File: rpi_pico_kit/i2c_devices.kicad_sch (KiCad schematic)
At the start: 7 parts, among them J7 Conn_01x04_Male, J8 OLED Display, J9 Conn_01x04_Male, U10 AT24CS32

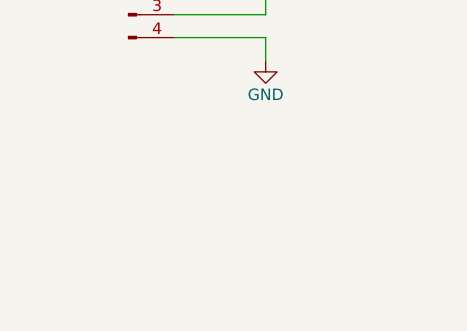
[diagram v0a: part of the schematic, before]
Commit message: added i2c interface for vga and dvi
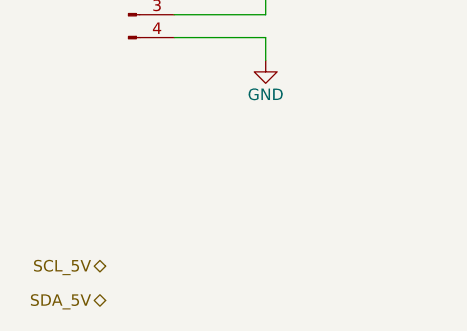
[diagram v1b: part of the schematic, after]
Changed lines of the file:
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@@
     (effects (font (size 1.27 1.27)) (justify right bottom))
+  )
+  (hierarchical_label "SDA_5V" (shape bidirectional) (at 81.28 143.51 180) (fields_autoplaced)
+    (effects (font (size 1.27 1.27)) (justify right))
+  )
+  (hierarchical_label "SCL_5V" (shape bidirectional) (at 81.28 139.7 180) (fields_autoplaced)
+    (effects (font (size 1.27 1.27)) (justify right))
   )
   (hierarchical_label "SDA" (shape bidirectional) (at 80.01 82.55 180) (fields_autoplaced)

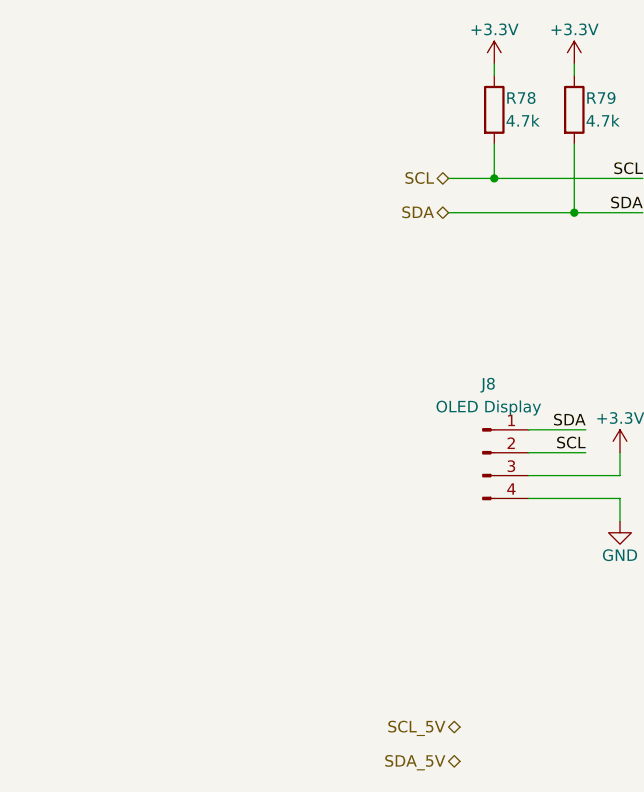
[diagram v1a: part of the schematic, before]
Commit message: added i2c level shifters
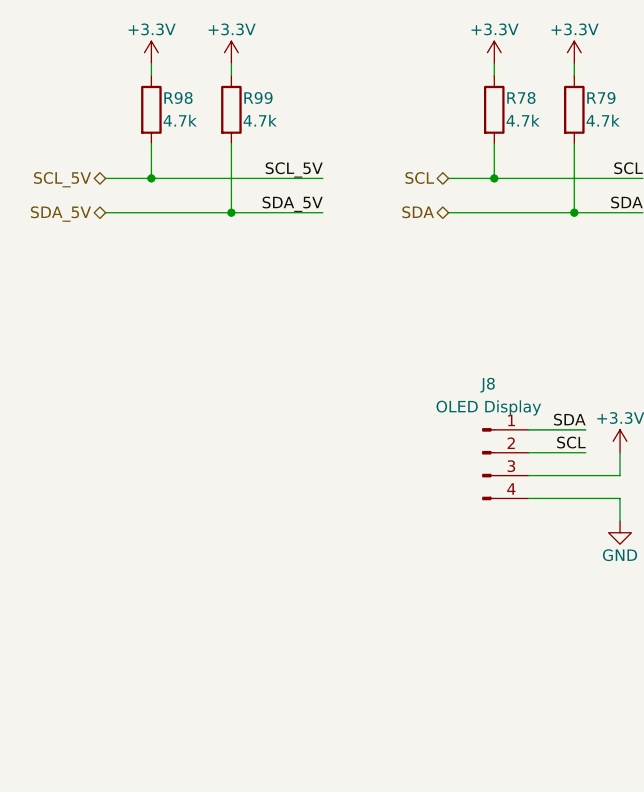
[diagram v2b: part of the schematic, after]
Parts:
- added R98, R99: 4.7k, Resistor_SMD:R_0805_2012Metric_Pad1.20x1.40mm_HandSolder, symbol Device:R
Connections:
- net +3V3: now also R98.1, R99.1
- net SCL_5V: now also R98.2
- net SDA_5V: now also R99.2
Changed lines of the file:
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@@
     (rev "1")
   )
+  (junction (at 46.99 78.74) (diameter 0) (color 0 0 0 0)
+  )
   (junction (at 209.55 86.36) (diameter 0) (color 0 0 0 0)
   )
@@
   (junction (at 93.98 82.55) (diameter 0) (color 0 0 0 0)
   )
+  (junction (at 55.88 82.55) (diameter 0) (color 0 0 0 0)
+  )
   (junction (at 85.09 78.74) (diameter 0) (color 0 0 0 0)
   )
@@
     (stroke (width 0) (type default))
   )
+  (wire (pts (xy 55.88 82.55) (xy 66.04 82.55))
+    (stroke (width 0) (type default))
+  )
   (wire (pts (xy 88.9 109.22) (xy 95.25 109.22))
     (stroke (width 0) (type default))
@@
     (stroke (width 0) (type default))
   )
+  (wire (pts (xy 41.91 78.74) (xy 46.99 78.74))
+    (stroke (width 0) (type default))
+  )
   (wire (pts (xy 219.71 101.6) (xy 222.25 101.6))
     (stroke (width 0) (type default))
@@
     (stroke (width 0) (type default))
   )
+  (wire (pts (xy 55.88 74.93) (xy 55.88 82.55))
+    (stroke (width 0) (type default))
+  )
   (wire (pts (xy 146.05 76.2) (xy 156.21 76.2))
     (stroke (width 0) (type default))
@@
     (stroke (width 0) (type default))
   )
+  (wire (pts (xy 46.99 78.74) (xy 66.04 78.74))
+    (stroke (width 0) (type default))
+  )
+  (wire (pts (xy 41.91 82.55) (xy 55.88 82.55))
+    (stroke (width 0) (type default))
+  )
+  (wire (pts (xy 46.99 66.04) (xy 46.99 67.31))
+    (stroke (width 0) (type default))
+  )
   (wire (pts (xy 219.71 96.52) (xy 229.87 96.52))
     (stroke (width 0) (type default))
@@
     (stroke (width 0) (type default))
   )
+  (wire (pts (xy 55.88 66.04) (xy 55.88 67.31))
+    (stroke (width 0) (type default))
+  )
   (wire (pts (xy 209.55 81.28) (xy 209.55 86.36))
     (stroke (width 0) (type default))
@@
     (stroke (width 0) (type default))
   )
+  (wire (pts (xy 46.99 74.93) (xy 46.99 78.74))
+    (stroke (width 0) (type default))
+  )
   (wire (pts (xy 199.39 96.52) (xy 196.85 96.52))
     (stroke (width 0) (type default))
@@
     (effects (font (size 1.27 1.27)) (justify right bottom))
   )
+  (label "SCL_5V" (at 66.04 78.74 0) (fields_autoplaced)
+    (effects (font (size 1.27 1.27)) (justify right bottom))
+  )
   (label "SCL" (at 156.21 109.22 0) (fields_autoplaced)
     (effects (font (size 1.27 1.27)) (justify right bottom))
@@
     (effects (font (size 1.27 1.27)) (justify right bottom))
   )
+  (label "SDA_5V" (at 66.04 82.55 0) (fields_autoplaced)
+    (effects (font (size 1.27 1.27)) (justify right bottom))
+  )
   (label "SDA" (at 156.21 81.28 0) (fields_autoplaced)
     (effects (font (size 1.27 1.27)) (justify right bottom))
   )
-  (hierarchical_label "SDA_5V" (shape bidirectional) (at 81.28 143.51 180) (fields_autoplaced)
+  (hierarchical_label "SDA_5V" (shape bidirectional) (at 41.91 82.55 180) (fields_autoplaced)
     (effects (font (size 1.27 1.27)) (justify right))
   )
-  (hierarchical_label "SCL_5V" (shape bidirectional) (at 81.28 139.7 180) (fields_autoplaced)
+  (hierarchical_label "SCL_5V" (shape bidirectional) (at 41.91 78.74 180) (fields_autoplaced)
     (effects (font (size 1.27 1.27)) (justify right))
   )
@@
     (effects (font (size 1.27 1.27)) (justify right))
   )
+  (symbol (lib_id "power:+3.3V") (at 46.99 66.04 0) (unit 1)
+    (in_bom yes) (on_board yes)
+    (property "Reference" "#PWR087" (id 0) (at 46.99 69.85 0)
+      (effects (font (size 1.27 1.27)) hide)
+    )
+    (property "Value" "+3.3V" (id 1) (at 46.99 62.23 0)
+      (effects (font (size 1.27 1.27)))
+    )
+    (property "Footprint" "" (id 2) (at 46.99 66.04 0)
+      (effects (font (size 1.27 1.27)) hide)
+    )
+    (property "Datasheet" "" (id 3) (at 46.99 66.04 0)
+      (effects (font (size 1.27 1.27)) hide)
+    )
+    (pin "1")
+  )
   (symbol (lib_id "Device:C") (at 217.17 86.36 90) (unit 1)
     (in_bom yes) (on_board yes)
@@
     )
     (property "Datasheet" "~" (id 3) (at 93.98 71.12 0)
+      (effects (font (size 1.27 1.27)) hide)
+    )
+    (pin "1")
+    (pin "2")
+  )
+  (symbol (lib_id "power:+3.3V") (at 55.88 66.04 0) (unit 1)
+    (in_bom yes) (on_board yes)
+    (property "Reference" "#PWR088" (id 0) (at 55.88 69.85 0)
+      (effects (font (size 1.27 1.27)) hide)
+    )
+    (property "Value" "+3.3V" (id 1) (at 55.88 62.23 0)
+      (effects (font (size 1.27 1.27)))
+    )
+    (property "Footprint" "" (id 2) (at 55.88 66.04 0)
+      (effects (font (size 1.27 1.27)) hide)
+    )
+    (property "Datasheet" "" (id 3) (at 55.88 66.04 0)
+      (effects (font (size 1.27 1.27)) hide)
+    )
+    (pin "1")
+  )
+  (symbol (lib_id "Device:R") (at 46.99 71.12 0) (unit 1)
+    (in_bom yes) (on_board yes)
+    (property "Reference" "R98" (id 0) (at 48.26 69.85 0)
+      (effects (font (size 1.27 1.27)) (justify left))
+    )
+    (property "Value" "4.7k" (id 1) (at 48.26 72.39 0)
+      (effects (font (size 1.27 1.27)) (justify left))
+    )
+    (property "Footprint" "Resistor_SMD:R_0805_2012Metric_Pad1.20x1.40mm_HandSolder" (id 2) (at 45.212 71.12 90)
+      (effects (font (size 1.27 1.27)) hide)
+    )
+    (property "Datasheet" "~" (id 3) (at 46.99 71.12 0)
       (effects (font (size 1.27 1.27)) hide)
     )
@@
     (pin "1")
   )
+  (symbol (lib_id "Device:R") (at 55.88 71.12 0) (unit 1)
+    (in_bom yes) (on_board yes)
+    (property "Reference" "R99" (id 0) (at 57.15 69.85 0)
+      (effects (font (size 1.27 1.27)) (justify left))
+    )
+    (property "Value" "4.7k" (id 1) (at 57.15 72.39 0)
+      (effects (font (size 1.27 1.27)) (justify left))
+    )
+    (property "Footprint" "Resistor_SMD:R_0805_2012Metric_Pad1.20x1.40mm_HandSolder" (id 2) (at 54.102 71.12 90)
+      (effects (font (size 1.27 1.27)) hide)
+    )
+    (property "Datasheet" "~" (id 3) (at 55.88 71.12 0)
+      (effects (font (size 1.27 1.27)) hide)
+    )
+    (pin "1")
+    (pin "2")
+  )
   (symbol (lib_id "power:GND") (at 196.85 104.14 0) (unit 1)

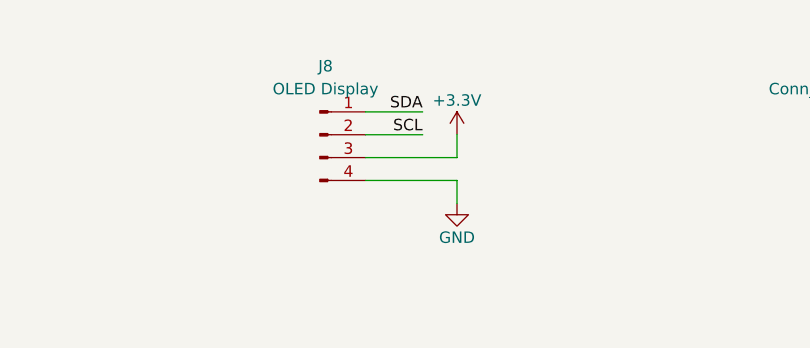
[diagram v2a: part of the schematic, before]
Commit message: added test pads for uart and swd of debugger
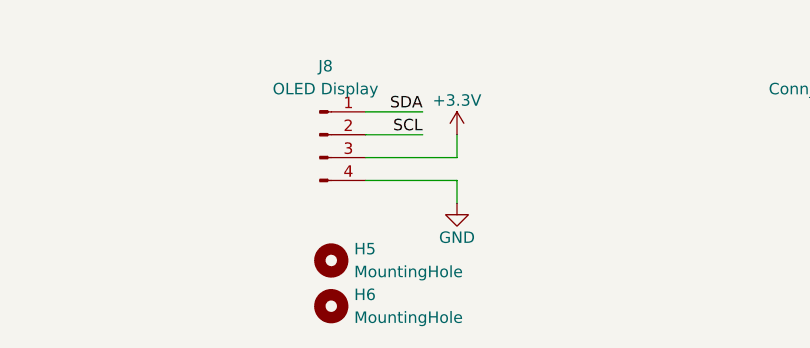
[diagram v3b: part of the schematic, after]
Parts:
- added H5, H6: MountingHole, MountingHole:MountingHole_2.7mm_M2.5, symbol Mechanical:MountingHole
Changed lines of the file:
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@@
     (effects (font (size 1.27 1.27)) (justify right))
+  )
+  (symbol (lib_id "Mechanical:MountingHole") (at 85.09 128.27 0) (unit 1)
+    (in_bom yes) (on_board yes) (fields_autoplaced)
+    (property "Reference" "H6" (id 0) (at 87.63 126.9999 0)
+      (effects (font (size 1.27 1.27)) (justify left))
+    )
+    (property "Value" "MountingHole" (id 1) (at 87.63 129.5399 0)
+      (effects (font (size 1.27 1.27)) (justify left))
+    )
+    (property "Footprint" "MountingHole:MountingHole_2.7mm_M2.5" (id 2) (at 85.09 128.27 0)
+      (effects (font (size 1.27 1.27)) hide)
+    )
+    (property "Datasheet" "~" (id 3) (at 85.09 128.27 0)
+      (effects (font (size 1.27 1.27)) hide)
+    )
   )
   (symbol (lib_id "power:+3.3V") (at 46.99 66.04 0) (unit 1)
@@
     (pin "1")
   )
+  (symbol (lib_id "Mechanical:MountingHole") (at 85.09 123.19 0) (unit 1)
+    (in_bom yes) (on_board yes) (fields_autoplaced)
+    (property "Reference" "H5" (id 0) (at 87.63 121.9199 0)
+      (effects (font (size 1.27 1.27)) (justify left))
+    )
+    (property "Value" "MountingHole" (id 1) (at 87.63 124.4599 0)
+      (effects (font (size 1.27 1.27)) (justify left))
+    )
+    (property "Footprint" "MountingHole:MountingHole_2.7mm_M2.5" (id 2) (at 85.09 123.19 0)
+      (effects (font (size 1.27 1.27)) hide)
+    )
+    (property "Datasheet" "~" (id 3) (at 85.09 123.19 0)
+      (effects (font (size 1.27 1.27)) hide)
+    )
+  )
 )

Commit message: added some MPNs, added fiducials
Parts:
- U10: Manufacturer Part Number (none) -> CAT24C32WI-GT3; Supplier (none) -> Digikey; Supplier Part URL (none) -> https://www.digikey.cz/en/products/detail/onsemi/CAT24C32WI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
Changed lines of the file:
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@@
+      (effects (font (size 1.27 1.27)) hide)
+    )
+    (property "Manufacturer Part Number" "CAT24C32WI-GT3" (id 4) (at 209.55 99.06 0)
+      (effects (font (size 1.27 1.27)) hide)
+    )
+    (property "Supplier" "Digikey" (id 5) (at 209.55 99.06 0)
+      (effects (font (size 1.27 1.27)) hide)
+    )
+    (property "Supplier Part URL" "https://www.digikey.cz/en/products/detail/onsemi/CAT24C32WI-GT3/1631007" (id 6) (at 209.55 99.06 0)
       (effects (font (size 1.27 1.27)) hide)
     )

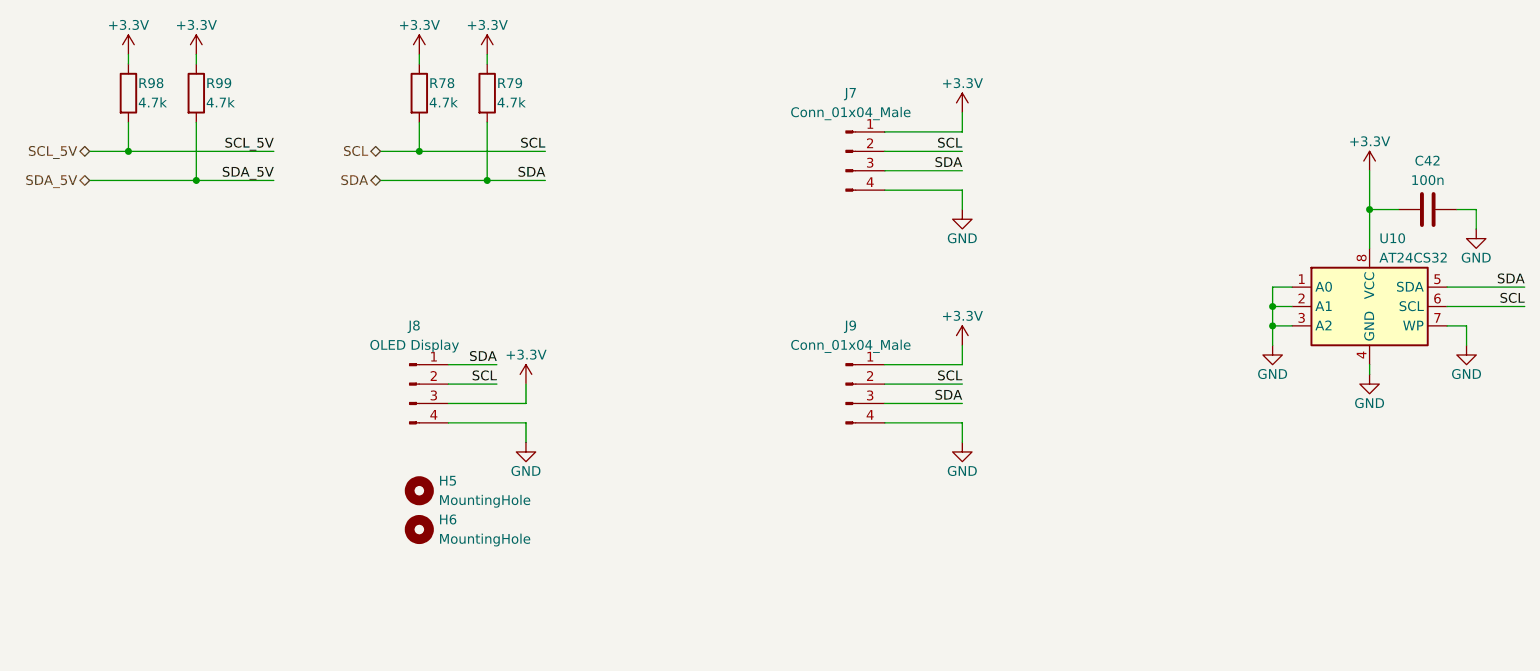
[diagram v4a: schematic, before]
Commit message: edited 5V I2C, added some footprints, MPNs, added HDMI footprint library
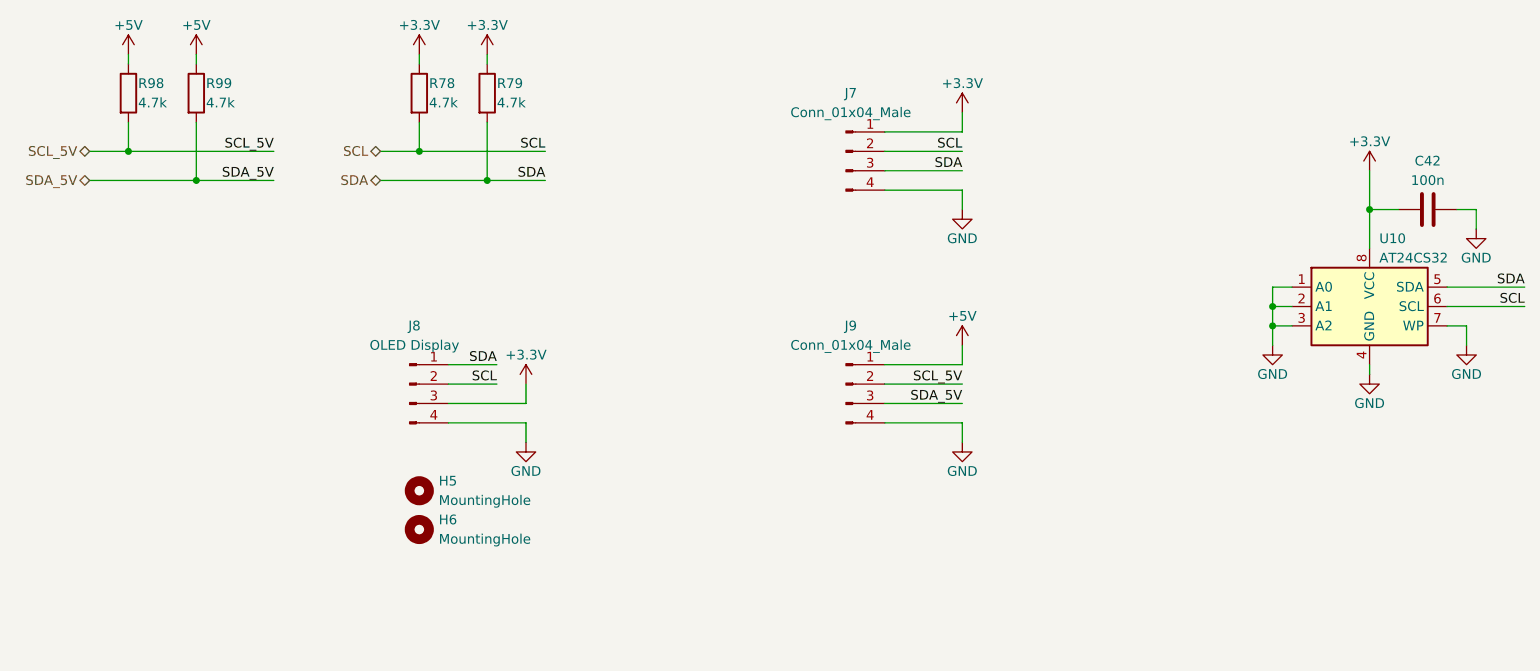
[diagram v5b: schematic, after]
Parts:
- J7, J9: footprint (none) -> Connector_PinHeader_2.54mm:PinHeader_1x04_P2.54mm_Vertical
- J8: footprint Display:Adafruit_SSD1306 -> (none)
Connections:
- net +3V3: no longer J9.1 (Pin_1), R98.1, R99.1
- net SCL: no longer J9.2 (Pin_2)
- net SCL_5V: now also J9.2 (Pin_2)
- net SDA: no longer J9.3 (Pin_3)
- net SDA_5V: now also J9.3 (Pin_3)
- new net +5V: J9.1 (Pin_1), R98.1, R99.1

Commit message: added some footprints and MPNs
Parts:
- J8: Manufacturer Part Number (none) -> LA141008DI; Supplier (none) -> Laskakit; Supplier Part URL (none) -> https://www.laskakit.cz/oled-displej-modry-a-zluty-128x64-0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
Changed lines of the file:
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@@
+      (effects (font (size 1.27 1.27)) hide)
+    )
+    (property "Manufacturer Part Number" "LA141008DI" (id 4) (at 83.82 109.22 0)
+      (effects (font (size 1.27 1.27)) hide)
+    )
+    (property "Supplier" "Laskakit" (id 5) (at 83.82 109.22 0)
+      (effects (font (size 1.27 1.27)) hide)
+    )
+    (property "Supplier Part URL" "https://www.laskakit.cz/oled-displej-modry-a-zluty-128x64-0-96--i2c/" (id 6) (at 83.82 109.22 0)
       (effects (font (size 1.27 1.27)) hide)
     )

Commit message: added MPNs for capacitors
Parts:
- C42: Manufacturer Part Number (none) -> C0805C104M3RAC7800; Supplier (none) -> Digikey; Supplier Part URL (none) -> https://www.digikey.cz/en/products/detail/kemet/C0805C104M3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
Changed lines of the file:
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@@
+      (effects (font (size 1.27 1.27)) hide)
+    )
+    (property "Manufacturer Part Number" "C0805C104M3RAC7800" (id 4) (at 217.17 86.36 0)
+      (effects (font (size 1.27 1.27)) hide)
+    )
+    (property "Supplier" "Digikey" (id 5) (at 217.17 86.36 0)
+      (effects (font (size 1.27 1.27)) hide)
+    )
+    (property "Supplier Part URL" "https://www.digikey.cz/en/products/detail/kemet/C0805C104M3RAC7800/2211748" (id 6) (at 217.17 86.36 0)
       (effects (font (size 1.27 1.27)) hide)
     )

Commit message: added MPNs for resistors
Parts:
- R78, R79, R98, R99: Manufacturer Part Number (none) -> RC0805FR-074K7L; Supplier (none) -> Digikey; Supplier Part URL (none) -> https://www.digikey.cz/en/products/detail/yageo/RC0805FR-07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
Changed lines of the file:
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@@
+      (effects (font (size 1.27 1.27)) hide)
+    )
+    (property "Manufacturer Part Number" "RC0805FR-074K7L" (id 4) (at 93.98 71.12 0)
+      (effects (font (size 1.27 1.27)) hide)
+    )
+    (property "Supplier" "Digikey" (id 5) (at 93.98 71.12 0)
+      (effects (font (size 1.27 1.27)) hide)
+    )
+    (property "Supplier Part URL" "https://www.digikey.cz/en/products/detail/yageo/RC0805FR-074K7L/727929" (id 6) (at 93.98 71.12 0)
       (effects (font (size 1.27 1.27)) hide)
     )
@@
     )
     (property "Datasheet" "~" (id 3) (at 46.99 71.12 0)
+      (effects (font (size 1.27 1.27)) hide)
+    )
+    (property "Manufacturer Part Number" "RC0805FR-074K7L" (id 4) (at 46.99 71.12 0)
+      (effects (font (size 1.27 1.27)) hide)
+    )
+    (property "Supplier" "Digikey" (id 5) (at 46.99 71.12 0)
+      (effects (font (size 1.27 1.27)) hide)
+    )
+    (property "Supplier Part URL" "https://www.digikey.cz/en/products/detail/yageo/RC0805FR-074K7L/727929" (id 6) (at 46.99 71.12 0)
       (effects (font (size 1.27 1.27)) hide)
     )
@@
       (effects (font (size 1.27 1.27)) hide)
     )
+    (property "Manufacturer Part Number" "RC0805FR-074K7L" (id 4) (at 85.09 71.12 0)
+      (effects (font (size 1.27 1.27)) hide)
+    )
+    (property "Supplier" "Digikey" (id 5) (at 85.09 71.12 0)
+      (effects (font (size 1.27 1.27)) hide)
+    )
+    (property "Supplier Part URL" "https://www.digikey.cz/en/products/detail/yageo/RC0805FR-074K7L/727929" (id 6) (at 85.09 71.12 0)
+      (effects (font (size 1.27 1.27)) hide)
+    )
     (pin "1")
     (pin "2")
@@
       (effects (font (size 1.27 1.27)) hide)
     )
+    (property "Manufacturer Part Number" "RC0805FR-074K7L" (id 4) (at 55.88 71.12 0)
+      (effects (font (size 1.27 1.27)) hide)
+    )
+    (property "Supplier" "Digikey" (id 5) (at 55.88 71.12 0)
+      (effects (font (size 1.27 1.27)) hide)
+    )
+    (property "Supplier Part URL" "https://www.digikey.cz/en/products/detail/yageo/RC0805FR-074K7L/727929" (id 6) (at 55.88 71.12 0)
+      (effects (font (size 1.27 1.27)) hide)
+    )
